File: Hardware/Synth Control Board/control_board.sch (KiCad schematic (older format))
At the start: 50 parts, among them J1 Conn_02x13_Odd_Even, J10 Conn_01x05, J11 Conn_01x08, J2 Conn_01x03, J3 Conn_02x13_Odd_Even, J5 Conn_01x08, J7 Conn_01x05, J8 Conn_01x05, J9 Conn_01x05, SW1 SW_DPDT_x2, SW10 SW_SPST, SW11 SW_SPST, SW12 SW_SPST, SW13 SW_SPST, SW2 SW_SPST, SW3 SW_SPST, SW4 SW_SPST, SW5 SW_SPST, SW6 SW_SPDT, SW7 SW_SPDT, SW8 SW_SPDT, SW9 SW_SPDT

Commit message: temporary global feedback control
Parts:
- removed J5: Conn_01x08, Pin_Headers:Pin_Header_Straight_1x08_Pitch2.54mm, symbol Conn_01x08
- added C?: C_Small, symbol C_Small
- added J?: Conn_01x08, Pin_Headers:Pin_Header_Straight_1x08_Pitch2.54mm, symbol Conn_01x08
- added R?: R, symbol R
- added RV29: 10kA, Potentiometers:Potentiometer_Bourns_PTV09A-1_Horizontal, symbol POT
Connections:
- net GND: now also RV29.3
- net LFO_freq_in: now also J?.7 (Pin_7)
- net LFO_freq_out: now also J?.8 (Pin_8)
- net freq_fb_2: no longer RV15.3, RV15.4, RV15.5
- new net: RV15.3, RV15.4, RV15.5
- new net: R?.1, RV29.1
- new net: C?.2, RV29.2
- new net delay_fb_in: J?.1 (Pin_1)
- new net delay_fb_out: J?.2 (Pin_2)
- new net delay_in: C?.1, J?.5 (Pin_5), R?.2
- new net delay_out: J?.6 (Pin_6)
- new net delay_time_in: J?.3 (Pin_3)
- new net delay_time_out: J?.4 (Pin_4)
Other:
- moved on the sheet: RV5

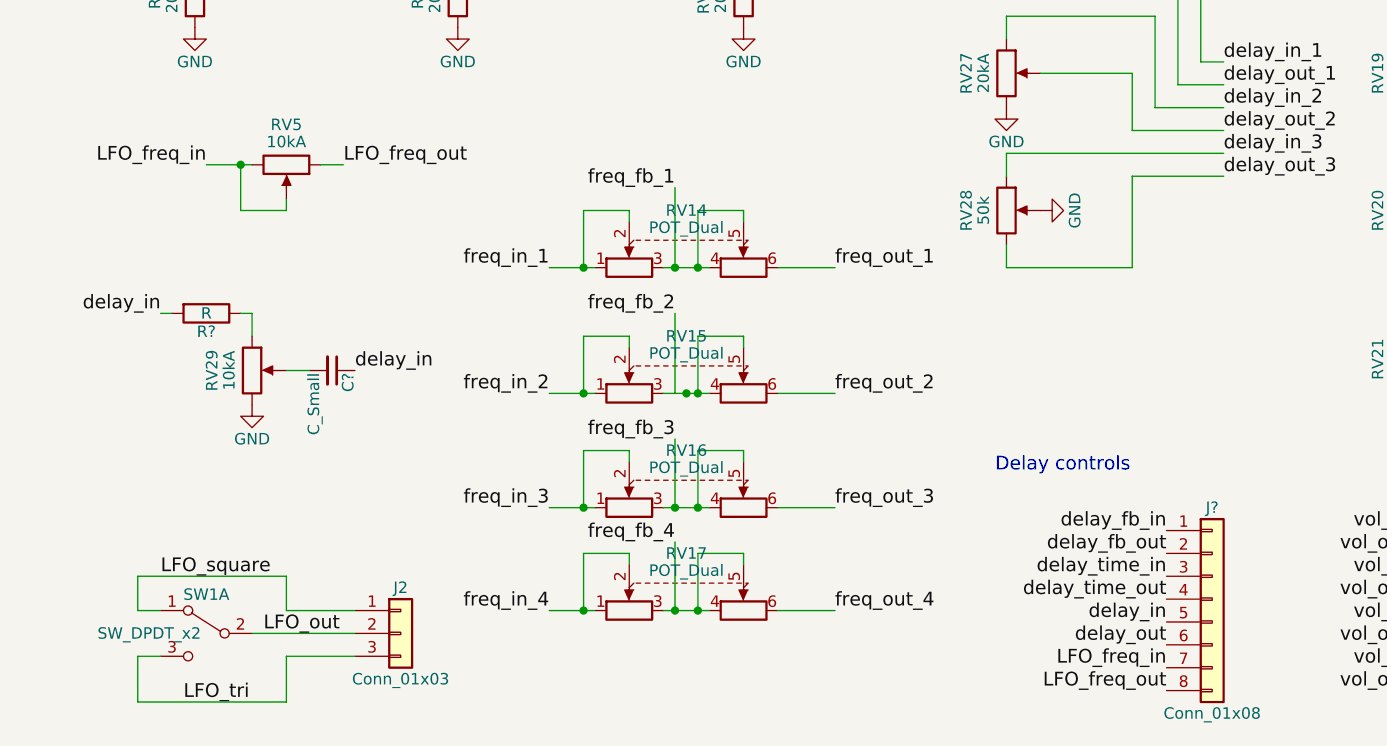
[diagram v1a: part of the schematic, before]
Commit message: fix filter pots. Dual ganged pot footprint was incorrect.
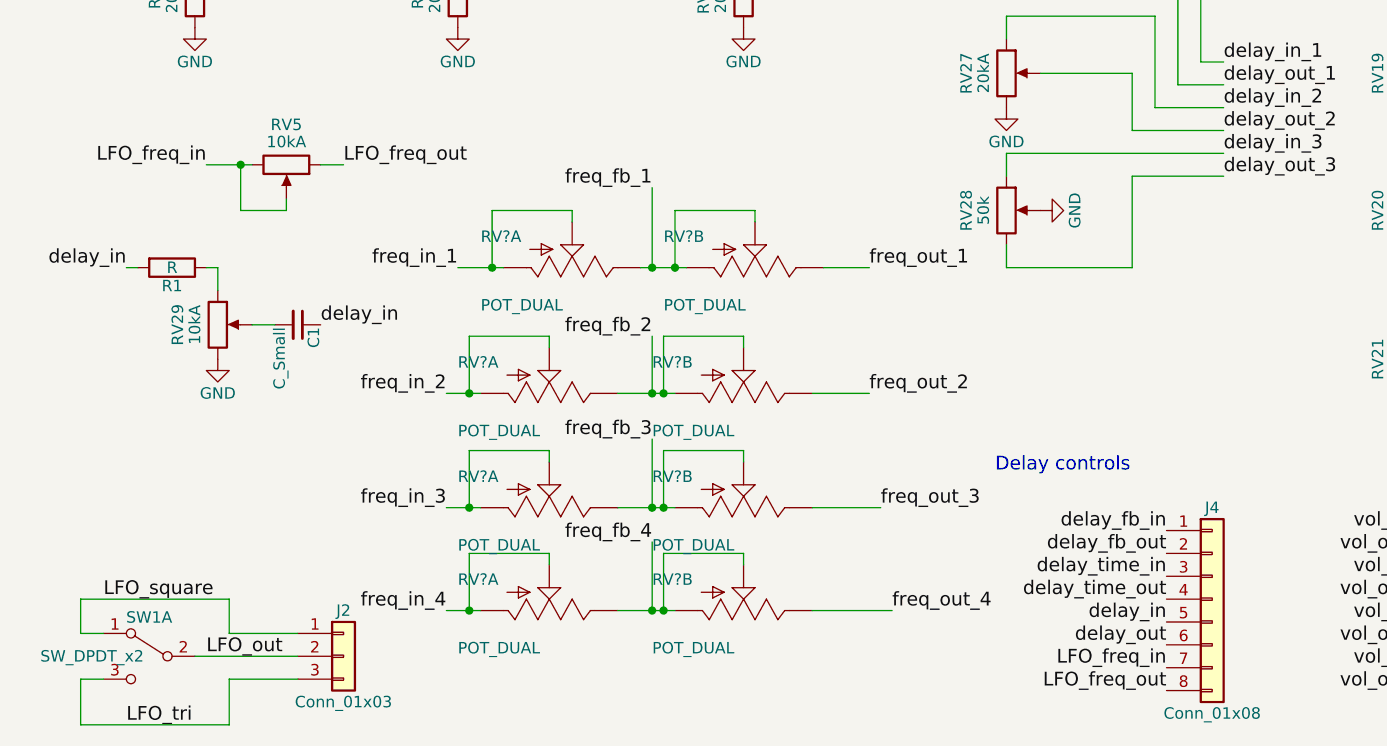
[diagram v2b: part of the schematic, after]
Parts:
- removed RV14, RV15, RV16, RV17: POT_Dual, Potentiometers:Potentiometer_Alps_RK09L_Double_Horizontal, symbol POT_Dual
- added RV? (x8): POT_DUAL, SparkFun-Electromechanical:POT_PANASONIC_DUAL_VERT_KIT, symbol POT_DUAL
- C1: renamed from C?; footprint (none) -> digikey-footprints:0805
- R1: renamed from R?; footprint (none) -> digikey-footprints:0805
- gave numbers to parts that had none: 1
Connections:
- net freq_fb_1: now also RV?.A1 (E), RV?.B2 (S), RV?.B3 (A)
- net freq_fb_2: now also RV?.A1 (E), RV?.B2 (S), RV?.B3 (A)
- net freq_fb_3: now also RV?.A1 (E), RV?.B2 (S), RV?.B3 (A)
- net freq_fb_4: now also RV?.A1 (E), RV?.B2 (S), RV?.B3 (A)
- net freq_in_1: now also RV?.A2 (S), RV?.A3 (A)
- net freq_in_2: now also RV?.A2 (S), RV?.A3 (A)
- net freq_in_3: now also RV?.A2 (S), RV?.A3 (A)
- net freq_in_4: now also RV?.A2 (S), RV?.A3 (A)
- net freq_out_1: now also RV?.B1 (E)
- net freq_out_2: now also RV?.B1 (E)
- net freq_out_3: now also RV?.B1 (E)
- net freq_out_4: now also RV?.B1 (E)
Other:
- moved on the sheet: C1, J2, R1, RV29, SW1A

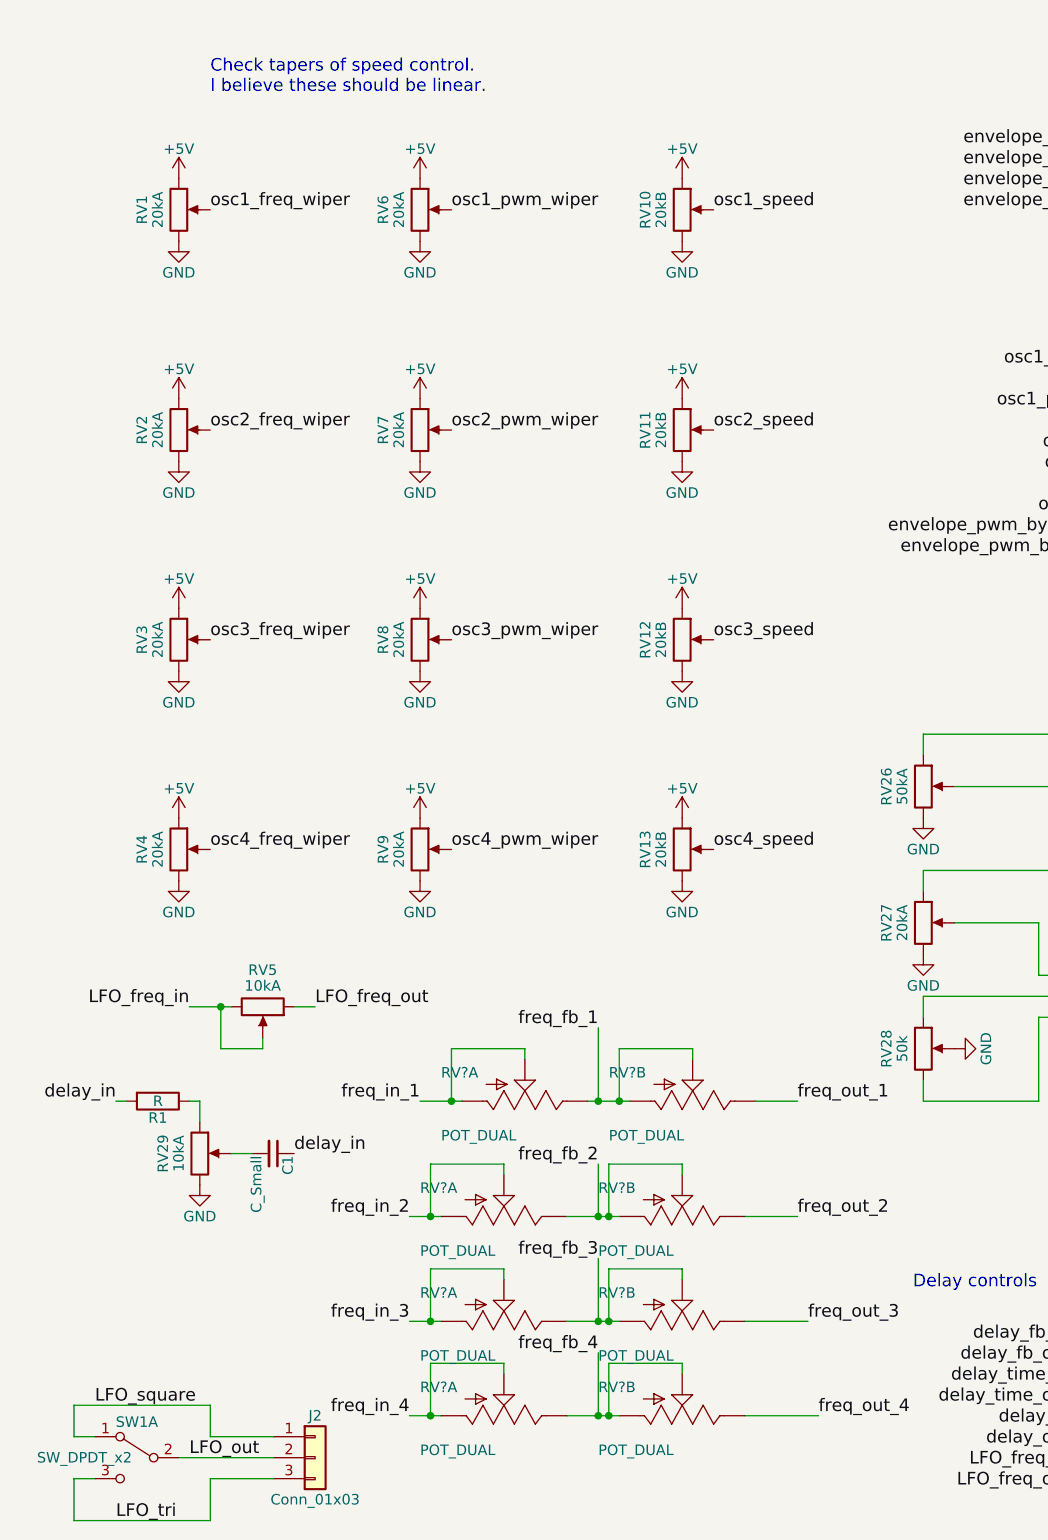
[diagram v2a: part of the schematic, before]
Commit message: add end stop resistors and reservoir caps to potentiometers.
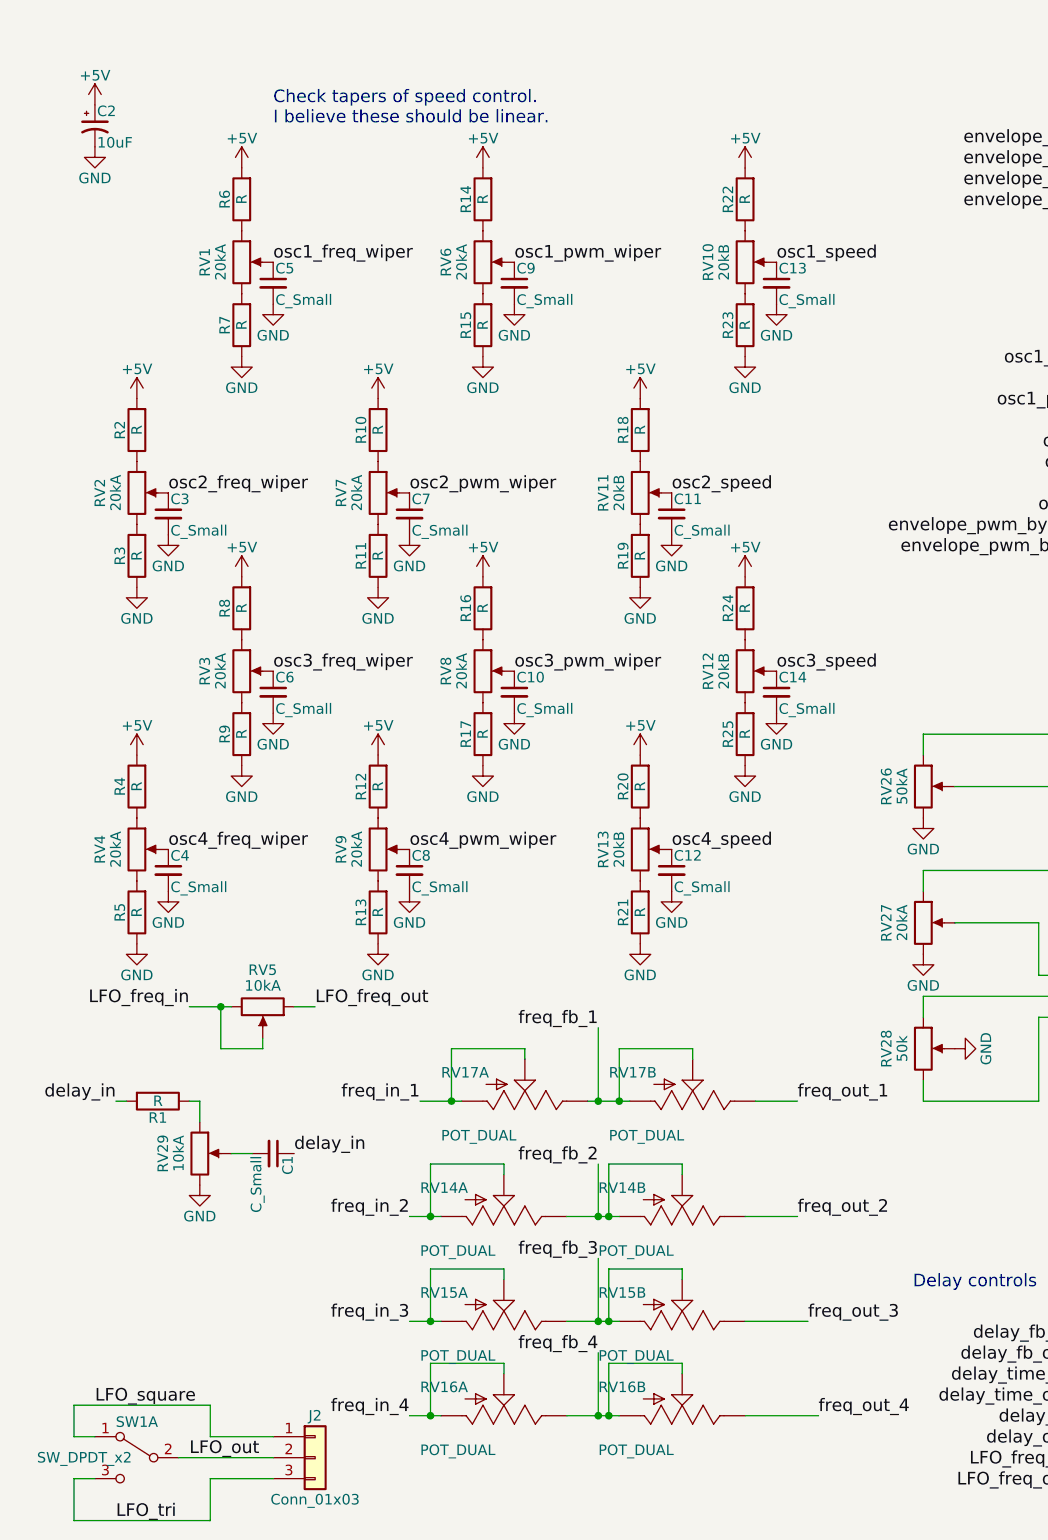
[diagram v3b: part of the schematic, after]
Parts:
- added C10, C11, C12, C13, C14, C3, C4, C5, C6, C7, C8, C9: C_Small, digikey-footprints:0805, symbol C_Small
- added C2: 10uF, Capacitors_THT:CP_Radial_D8.0mm_P5.00mm, symbol CP1_Small
- added R10, R11, R12, R13, R14, R15, R16, R17, R18, R19, R2, R20, R21, R22, R23, R24, R25, R3, R4, R5, R6, R7, R8, R9: R, digikey-footprints:0805, symbol R
- gave numbers to parts that had none: 4
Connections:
- net +5V: now also C2.1, R10.2, R12.2, R14.2, R16.2, R18.2, R2.2, R20.2, R22.2, R24.2, R4.2, R6.2, R8.2; no longer RV1.1, RV10.1, RV11.1, RV12.1, RV13.1, RV2.1, RV3.1, RV4.1, RV6.1, RV7.1, RV8.1, RV9.1
- net GND: now also C10.2, C11.2, C12.2, C13.2, C14.2, C2.2, C3.2, C4.2, C5.2, C6.2, C7.2, C8.2, C9.2, R11.1, R13.1, R15.1, R17.1, R19.1, R21.1, R23.1, R25.1, R3.1, R5.1, R7.1, R9.1; no longer RV1.3, RV10.3, RV11.3, RV12.3, RV13.3, RV2.3, RV3.3, RV4.3, RV6.3, RV7.3, RV8.3, RV9.3
- net osc1_freq_wiper: now also C5.1
- net osc1_pwm_wiper: now also C9.1
- net osc1_speed: now also C13.1
- net osc2_freq_wiper: now also C3.1
- net osc2_pwm_wiper: now also C7.1
- net osc2_speed: now also C11.1
- net osc3_freq_wiper: now also C6.1
- net osc3_pwm_wiper: now also C10.1
- net osc3_speed: now also C14.1
- net osc4_freq_wiper: now also C4.1
- net osc4_pwm_wiper: now also C8.1
- net osc4_speed: now also C12.1
- new net: R6.1, RV1.1
- new net: R7.2, RV1.3
- new net: R14.1, RV6.1
- new net: R15.2, RV6.3
- new net: R2.1, RV2.1
- new net: R3.2, RV2.3
- new net: R10.1, RV7.1
- new net: R11.2, RV7.3
- new net: R8.1, RV3.1
- new net: R9.2, RV3.3
- new net: R16.1, RV8.1
- new net: R17.2, RV8.3
- new net: R4.1, RV4.1
- new net: R5.2, RV4.3
- new net: R12.1, RV9.1
- new net: R13.2, RV9.3
- new net: R22.1, RV10.1
- new net: R23.2, RV10.3
- new net: R18.1, RV11.1
- new net: R19.2, RV11.3
- new net: R24.1, RV12.1
- new net: R25.2, RV12.3
- new net: R20.1, RV13.1
- new net: R21.2, RV13.3
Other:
- moved on the sheet: RV1, RV10, RV11, RV12, RV13, RV2, RV3, RV4, RV6, RV7, RV8, RV9

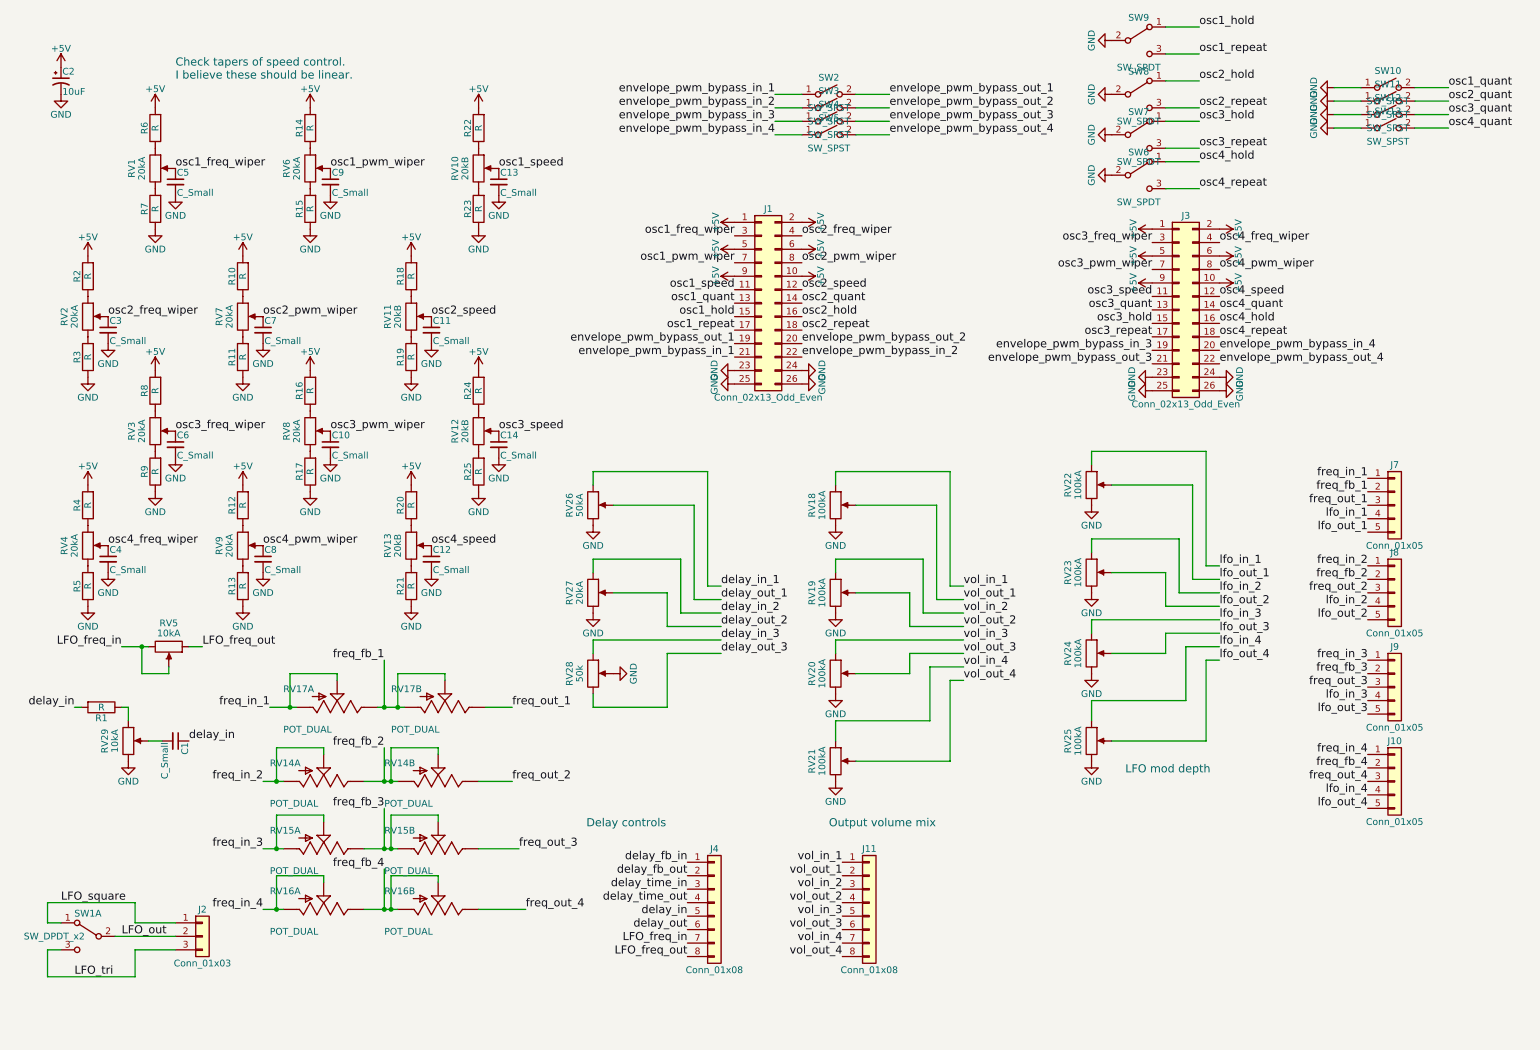
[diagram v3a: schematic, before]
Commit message: fix toggle switch footprints
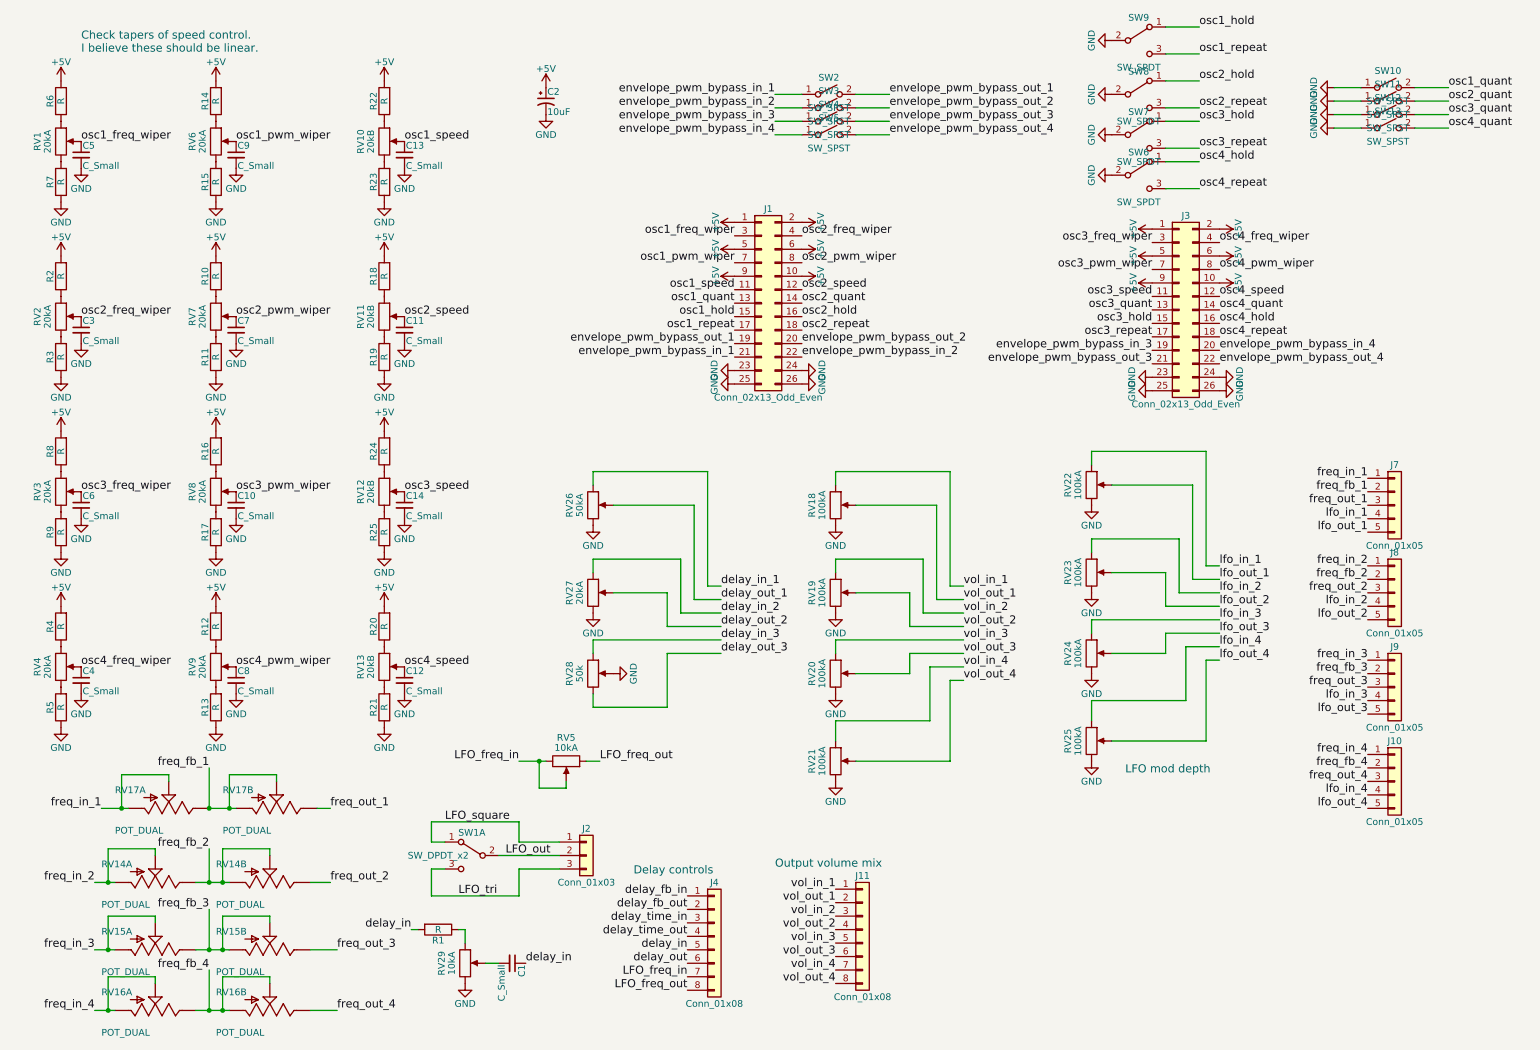
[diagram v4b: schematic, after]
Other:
- moved on the sheet: C1, C10, C11, C12, C13, C14, C2, C3, C4, C5, C6, C7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
